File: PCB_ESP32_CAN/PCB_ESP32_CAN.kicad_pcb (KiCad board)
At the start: 2 copper layers, 52.2 x 67.2 mm, 53 parts, among them J1 USB_C_Receptacle_USB2.0, J2 CAN, J3 CAN, J4 CAN, J5 CAN, Q1 Q_NPN_BCE, Q2 Q_NPN_BCE, U1 ESP32-WROOM-32, U2 CP2102N-A01-GQFN24, U3 SN65HVD232, U4 NCP1117-3.3_SOT223

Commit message: mod esp32
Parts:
- moved R8 0.10 mm to (64.1, 93.0)
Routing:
- net GND: vias 57 -> 131

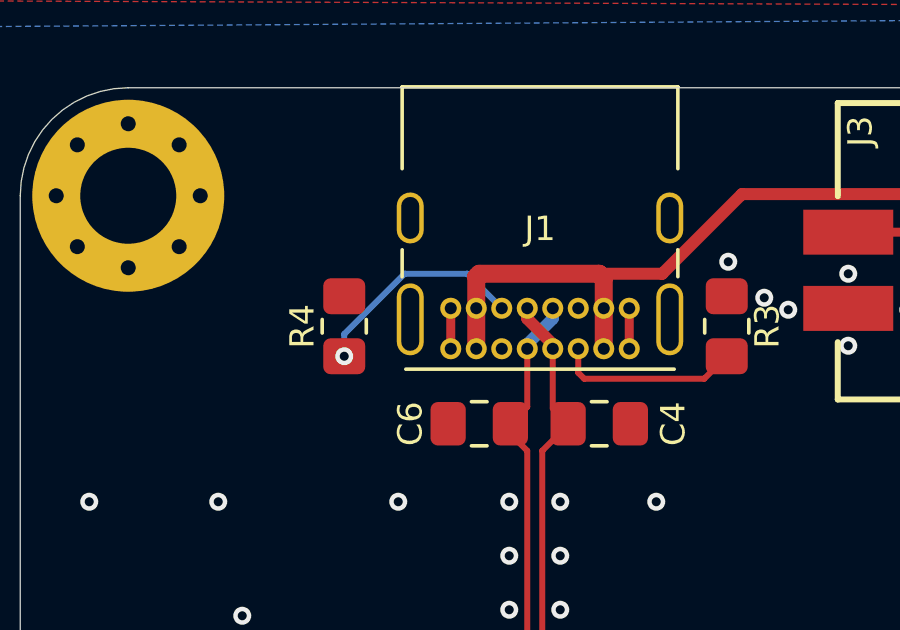
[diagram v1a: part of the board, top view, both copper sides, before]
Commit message: reroute some traces on ESP32 pcb
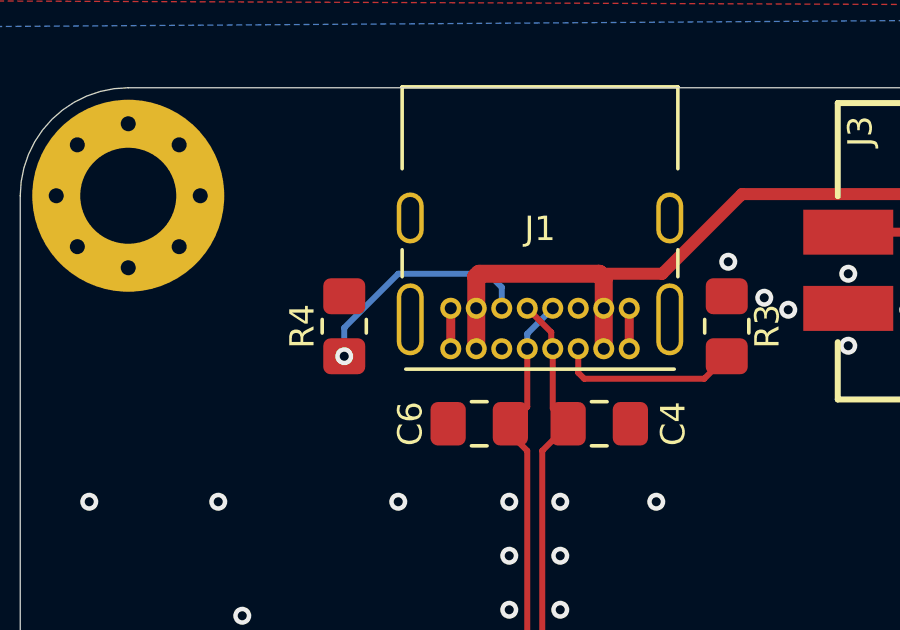
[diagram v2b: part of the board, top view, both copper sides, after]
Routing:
- net Net-(J1-PadB5): track 7.30 -> 7.83 mm
